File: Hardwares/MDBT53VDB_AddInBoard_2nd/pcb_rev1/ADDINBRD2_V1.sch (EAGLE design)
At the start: 17 parts, among them Q1 DMP2035UFDF-7, Q2 BC817-40QA, SW1 SKRPACE010, U1 SN74AHC1G00DRLR, U2 REF3325AIRSER, U3 MCP6232T-E/MNY

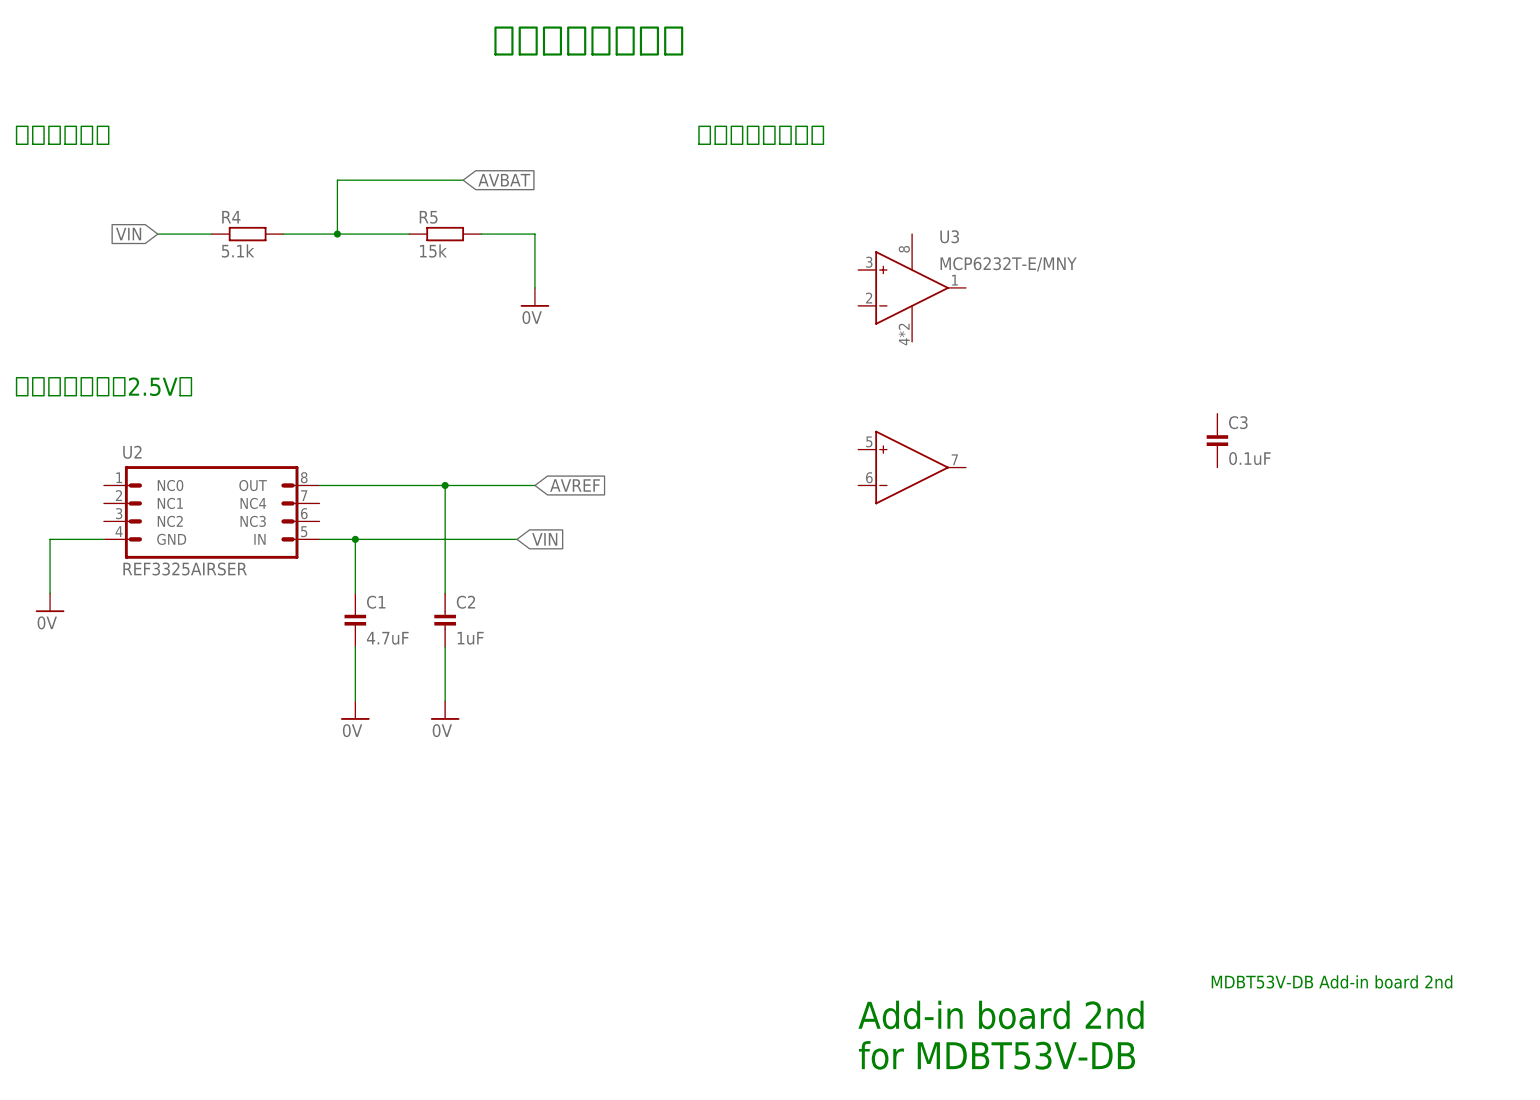
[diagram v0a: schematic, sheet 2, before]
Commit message: 回路図を修正
・オペアンプ周りの配線
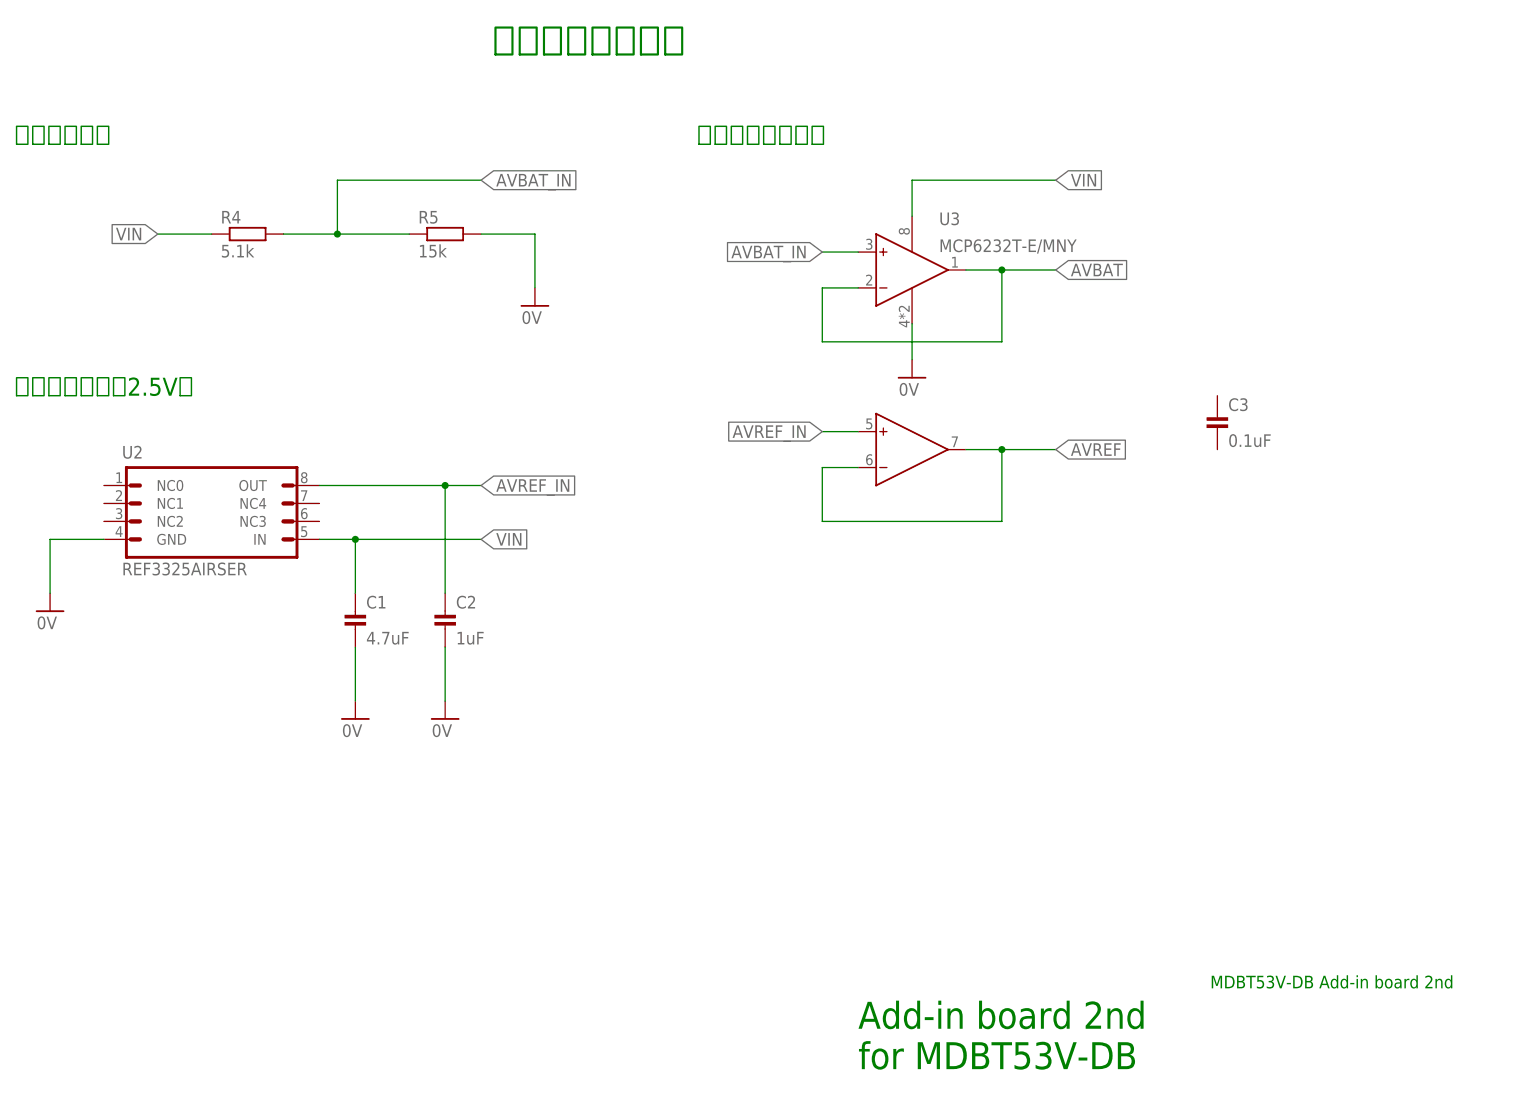
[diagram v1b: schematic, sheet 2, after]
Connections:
- new net AVBAT_IN: R4.2, R5.1, U3.VINA+
- new net AVREF_IN: C2.1, U2.OUT, U3.VINB+
- net 0V: now also U3.VSS
- net AVBAT: now also U3.VINA-, U3.VOUTA; no longer R4.2, R5.1
- net AVREF: now also U3.VINB-, U3.VOUTB; no longer C2.1, U2.OUT
- net VIN: now also U3.VDD
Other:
- moved on the sheet: C3, U3
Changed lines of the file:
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@@
 <part name="U1" library="ICs" deviceset="SN74AHC1G00" device="DRLR"/>
 <part name="U3" library="ICs" deviceset="MCP6232" device="T-E/MNY"/>
+<part name="GND9" library="Supply" deviceset="0V" device=""/>
 </parts>
 <sheets>
@@
 <instance part="R4" gate="G$1" x="81.28" y="127"/>
 <instance part="R5" gate="G$1" x="109.22" y="127"/>
-<instance part="C3" gate="G$1" x="218.44" y="99.06"/>
-<instance part="U3" gate="G$1" x="170.18" y="106.68"/>
+<instance part="C3" gate="G$1" x="218.44" y="101.6"/>
+<instance part="U3" gate="G$1" x="170.18" y="109.22"/>
+<instance part="GND9" gate="1" x="175.26" y="106.68"/>
 </instances>
 <busses>
@@
 <pinref part="U2" gate="G$1" pin="IN"/>
 <wire x1="91.44" y1="83.82" x2="96.52" y2="83.82" width="0.1524" layer="91"/>
-<label x="119.38" y="83.82" size="1.778" layer="95" xref="yes"/>
-<wire x1="96.52" y1="83.82" x2="119.38" y2="83.82" width="0.1524" layer="91"/>
+<label x="114.3" y="83.82" size="1.778" layer="95" xref="yes"/>
+<wire x1="96.52" y1="83.82" x2="114.3" y2="83.82" width="0.1524" layer="91"/>
 <junction x="96.52" y="83.82"/>
 <pinref part="C1" gate="G$1" pin="1"/>
 <wire x1="96.52" y1="83.82" x2="96.52" y2="76.2" width="0.1524" layer="91"/>
 </segment>
-</net>
-<net name="AVBAT" class="0">
+<segment>
+<pinref part="U3" gate="G$1" pin="VDD"/>
+<wire x1="175.26" y1="129.54" x2="175.26" y2="134.62" width="0.1524" layer="91"/>
+<wire x1="175.26" y1="134.62" x2="195.58" y2="134.62" width="0.1524" layer="91"/>
+<label x="195.58" y="134.62" size="1.778" layer="95" xref="yes"/>
+</segment>
+</net>
+<net name="AVBAT_IN" class="0">
 <segment>
 <wire x1="86.36" y1="127" x2="93.98" y2="127" width="0.1524" layer="91"/>
 <wire x1="93.98" y1="127" x2="104.14" y2="127" width="0.1524" layer="91"/>
 <wire x1="93.98" y1="127" x2="93.98" y2="134.62" width="0.1524" layer="91"/>
-<wire x1="93.98" y1="134.62" x2="111.76" y2="134.62" width="0.1524" layer="91"/>
+<wire x1="93.98" y1="134.62" x2="114.3" y2="134.62" width="0.1524" layer="91"/>
 <junction x="93.98" y="127"/>
-<label x="111.76" y="134.62" size="1.778" layer="95" xref="yes"/>
+<label x="114.3" y="134.62" size="1.778" layer="95" xref="yes"/>
 <pinref part="R4" gate="G$1" pin="2"/>
 <pinref part="R5" gate="G$1" pin="1"/>
+</segment>
+<segment>
+<pinref part="U3" gate="G$1" pin="VINA+"/>
+<wire x1="167.64" y1="124.46" x2="162.56" y2="124.46" width="0.1524" layer="91"/>
+<label x="162.56" y="124.46" size="1.778" layer="95" rot="R180" xref="yes"/>
 </segment>
 </net>
@@
 <wire x1="109.22" y1="68.58" x2="109.22" y2="60.96" width="0.1524" layer="91"/>
 </segment>
-</net>
-<net name="AVREF" class="0">
+<segment>
+<pinref part="GND9" gate="1" pin="0V"/>
+<pinref part="U3" gate="G$1" pin="VSS"/>
+<wire x1="175.26" y1="109.22" x2="175.26" y2="114.3" width="0.1524" layer="91"/>
+</segment>
+</net>
+<net name="AVREF_IN" class="0">
 <segment>
 <pinref part="U2" gate="G$1" pin="OUT"/>
 <wire x1="91.44" y1="91.44" x2="109.22" y2="91.44" width="0.1524" layer="91"/>
-<label x="121.92" y="91.44" size="1.778" layer="95" xref="yes"/>
-<wire x1="109.22" y1="91.44" x2="121.92" y2="91.44" width="0.1524" layer="91"/>
+<label x="114.3" y="91.44" size="1.778" layer="95" xref="yes"/>
+<wire x1="109.22" y1="91.44" x2="114.3" y2="91.44" width="0.1524" layer="91"/>
 <junction x="109.22" y="91.44"/>
 <pinref part="C2" gate="G$1" pin="1"/>
 <wire x1="109.22" y1="91.44" x2="109.22" y2="76.2" width="0.1524" layer="91"/>
 </segment>
-</net>
+<segment>
+<pinref part="U3" gate="G$1" pin="VINB+"/>
+<wire x1="167.64" y1="99.06" x2="162.56" y2="99.06" width="0.1524" layer="91"/>
+<label x="162.56" y="99.06" size="1.778" layer="95" rot="R180" xref="yes"/>
+</segment>
+</net>
+<net name="AVBAT" class="0">
+<segment>
+<pinref part="U3" gate="G$1" pin="VOUTA"/>
+<wire x1="182.88" y1="121.92" x2="187.96" y2="121.92" width="0.1524" layer="91"/>
+<label x="195.58" y="121.92" size="1.778" layer="95" xref="yes"/>
+<junction x="187.96" y="121.92"/>
+<wire x1="187.96" y1="121.92" x2="195.58" y2="121.92" width="0.1524" layer="91"/>
+<wire x1="187.96" y1="121.92" x2="187.96" y2="111.76" width="0.1524" layer="91"/>
+<wire x1="187.96" y1="111.76" x2="162.56" y2="111.76" width="0.1524" layer="91"/>
+<wire x1="162.56" y1="111.76" x2="162.56" y2="119.38" width="0.1524" layer="91"/>
+<pinref part="U3" gate="G$1" pin="VINA-"/>
+<wire x1="162.56" y1="119.38" x2="167.64" y2="119.38" width="0.1524" layer="91"/>
+</segment>
+</net>
+<net name="AVREF" class="0">
+<segment>
+<pinref part="U3" gate="G$1" pin="VOUTB"/>
+<wire x1="182.88" y1="96.52" x2="187.96" y2="96.52" width="0.1524" layer="91"/>
+<label x="195.58" y="96.52" size="1.778" layer="95" xref="yes"/>
+<junction x="187.96" y="96.52"/>
+<wire x1="187.96" y1="96.52" x2="195.58" y2="96.52" width="0.1524" layer="91"/>
+<wire x1="187.96" y1="96.52" x2="187.96" y2="86.36" width="0.1524" layer="91"/>
+<wire x1="187.96" y1="86.36" x2="162.56" y2="86.36" width="0.1524" layer="91"/>
+<wire x1="162.56" y1="86.36" x2="162.56" y2="93.98" width="0.1524" layer="91"/>
+<pinref part="U3" gate="G$1" pin="VINB-"/>
+<wire x1="162.56" y1="93.98" x2="167.64" y2="93.98" width="0.1524" layer="91"/>
+</segment>
+</net>

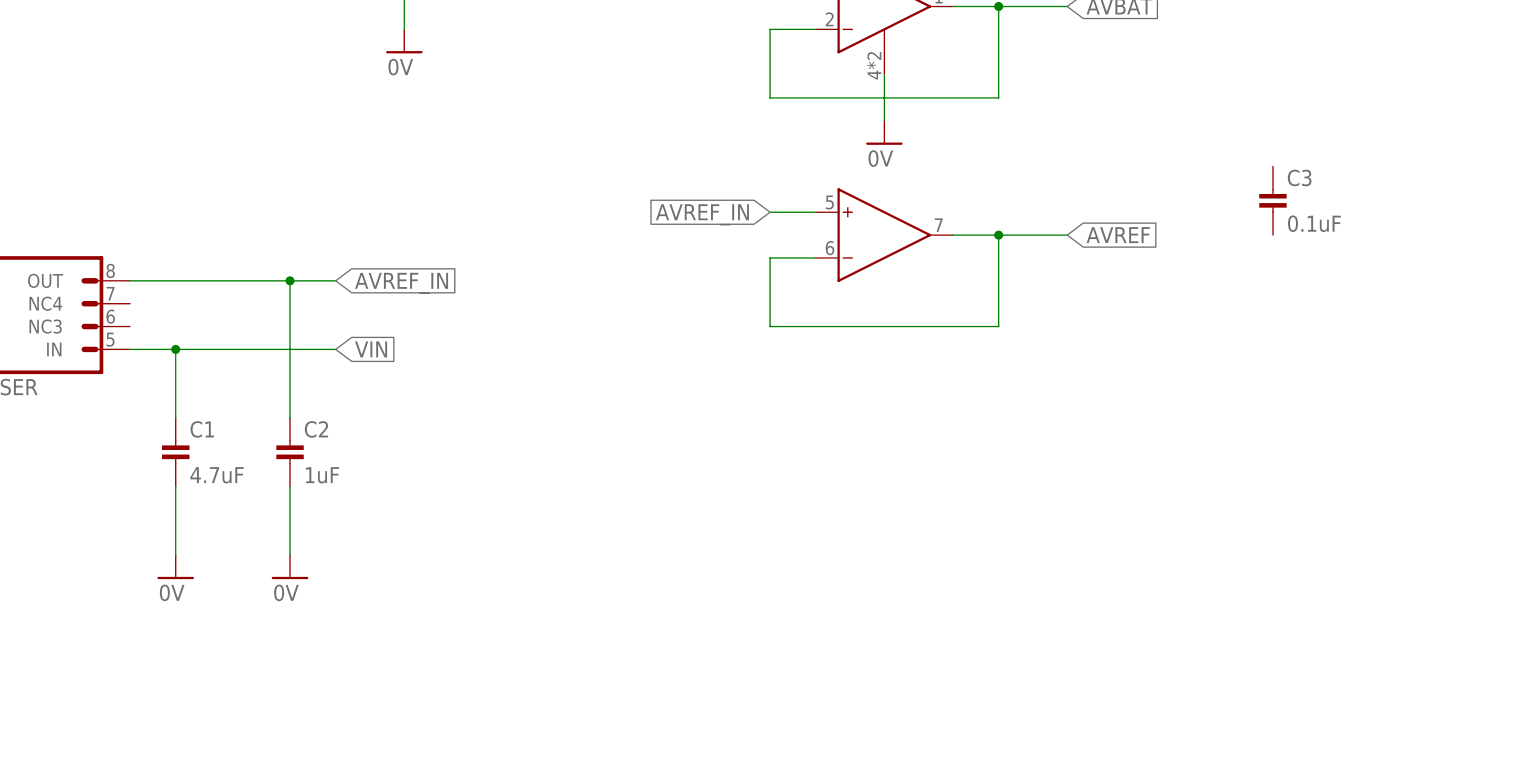
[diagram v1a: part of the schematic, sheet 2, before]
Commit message: 回路図を修正
・部品を入れ替え
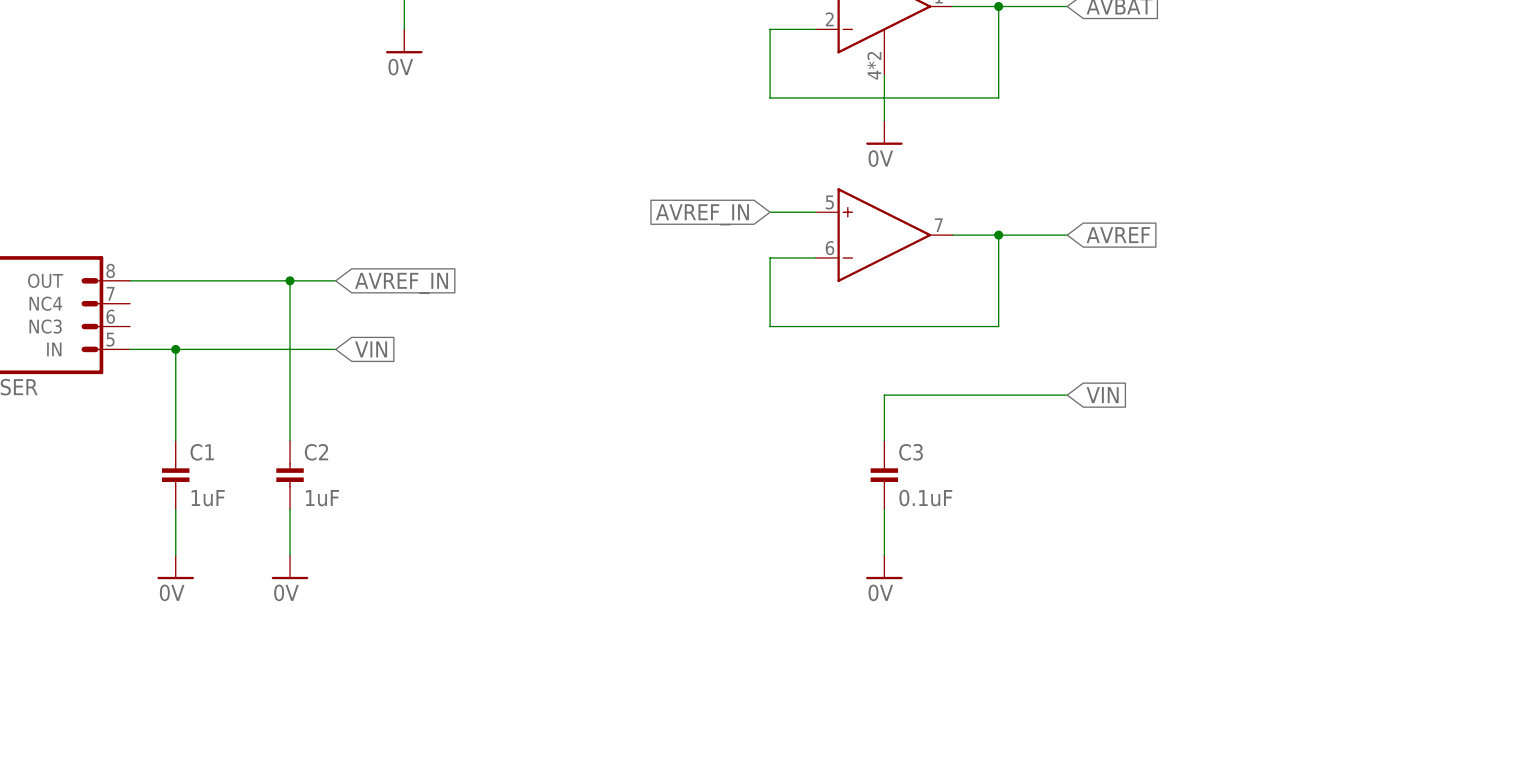
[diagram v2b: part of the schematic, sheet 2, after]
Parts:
- C1: value 4.7uF -> 1uF; device SMDs:JMK105BBJ475MVHF -> SMDs:TMK105AC6105KV-F
- C2: device SMDs:GRM155R70J105KA12J -> SMDs:TMK105AC6105KV-F
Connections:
- net 0V: now also C3.2
- net VIN: now also C3.1
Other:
- moved on the sheet: C1, C2, C3
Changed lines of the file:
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@@
 <part name="GND7" library="Supply" deviceset="0V" device=""/>
 <part name="GND8" library="Supply" deviceset="0V" device=""/>
-<part name="C1" library="SMDs" deviceset="JMK105BBJ" device="475MVHF" value="4.7uF"/>
-<part name="C2" library="SMDs" deviceset="GRM155" device="R70J105KA12J" value="1uF"/>
+<part name="C1" library="SMDs" deviceset="TMK105AC6" device="105KV-F" value="1uF"/>
+<part name="C2" library="SMDs" deviceset="TMK105AC6" device="105KV-F" value="1uF"/>
 <part name="R4" library="SMDs" deviceset="ERA-2A" device="PB512X" value="5.1k"/>
 <part name="R5" library="SMDs" deviceset="ERA-2A" device="PB153X" value="15k"/>
@@
 <part name="U3" library="ICs" deviceset="MCP6232" device="T-E/MNY"/>
 <part name="GND9" library="Supply" deviceset="0V" device=""/>
+<part name="GND11" library="Supply" deviceset="0V" device=""/>
 </parts>
 <sheets>
@@
 <instance part="GND7" gate="1" x="96.52" y="58.42"/>
 <instance part="GND8" gate="1" x="109.22" y="58.42"/>
-<instance part="C1" gate="G$1" x="96.52" y="73.66"/>
-<instance part="C2" gate="G$1" x="109.22" y="73.66"/>
+<instance part="C1" gate="G$1" x="96.52" y="71.12"/>
+<instance part="C2" gate="G$1" x="109.22" y="71.12"/>
 <instance part="R4" gate="G$1" x="81.28" y="127"/>
 <instance part="R5" gate="G$1" x="109.22" y="127"/>
-<instance part="C3" gate="G$1" x="218.44" y="101.6"/>
+<instance part="C3" gate="G$1" x="175.26" y="71.12"/>
 <instance part="U3" gate="G$1" x="170.18" y="109.22"/>
 <instance part="GND9" gate="1" x="175.26" y="106.68"/>
+<instance part="GND11" gate="1" x="175.26" y="58.42"/>
 </instances>
 <busses>
@@
 <junction x="96.52" y="83.82"/>
 <pinref part="C1" gate="G$1" pin="1"/>
-<wire x1="96.52" y1="83.82" x2="96.52" y2="76.2" width="0.1524" layer="91"/>
+<wire x1="96.52" y1="83.82" x2="96.52" y2="73.66" width="0.1524" layer="91"/>
 </segment>
 <segment>
@@
 <wire x1="175.26" y1="134.62" x2="195.58" y2="134.62" width="0.1524" layer="91"/>
 <label x="195.58" y="134.62" size="1.778" layer="95" xref="yes"/>
+</segment>
+<segment>
+<pinref part="C3" gate="G$1" pin="1"/>
+<wire x1="175.26" y1="73.66" x2="175.26" y2="78.74" width="0.1524" layer="91"/>
+<wire x1="175.26" y1="78.74" x2="195.58" y2="78.74" width="0.1524" layer="91"/>
+<label x="195.58" y="78.74" size="1.778" layer="95" xref="yes"/>
 </segment>
 </net>
@@
 <pinref part="C1" gate="G$1" pin="2"/>
 <pinref part="GND7" gate="1" pin="0V"/>
-<wire x1="96.52" y1="68.58" x2="96.52" y2="60.96" width="0.1524" layer="91"/>
+<wire x1="96.52" y1="66.04" x2="96.52" y2="60.96" width="0.1524" layer="91"/>
 </segment>
 <segment>
 <pinref part="C2" gate="G$1" pin="2"/>
 <pinref part="GND8" gate="1" pin="0V"/>
-<wire x1="109.22" y1="68.58" x2="109.22" y2="60.96" width="0.1524" layer="91"/>
+<wire x1="109.22" y1="66.04" x2="109.22" y2="60.96" width="0.1524" layer="91"/>
 </segment>
 <segment>
@@
 <pinref part="U3" gate="G$1" pin="VSS"/>
 <wire x1="175.26" y1="109.22" x2="175.26" y2="114.3" width="0.1524" layer="91"/>
+</segment>
+<segment>
+<pinref part="GND11" gate="1" pin="0V"/>
+<pinref part="C3" gate="G$1" pin="2"/>
+<wire x1="175.26" y1="60.96" x2="175.26" y2="66.04" width="0.1524" layer="91"/>
 </segment>
 </net>
@@
 <junction x="109.22" y="91.44"/>
 <pinref part="C2" gate="G$1" pin="1"/>
-<wire x1="109.22" y1="91.44" x2="109.22" y2="76.2" width="0.1524" layer="91"/>
-</segment>
-<segment>
+<wire x1="109.22" y1="91.44" x2="109.22" y2="73.66" width="0.1524" layer="91"/>
+</segment>
+<segment>
